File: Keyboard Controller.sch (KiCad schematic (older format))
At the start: 48 parts, among them SW1 SW_Push, SW2 SW_Push, SW3 SW_Push, SW4 SW_Push, SW5 SW_Push, SW6 SW_Push, SW7 SW_Push, SW8 SW_Push, SW9 SW_Push, U1 Teensy-3.2

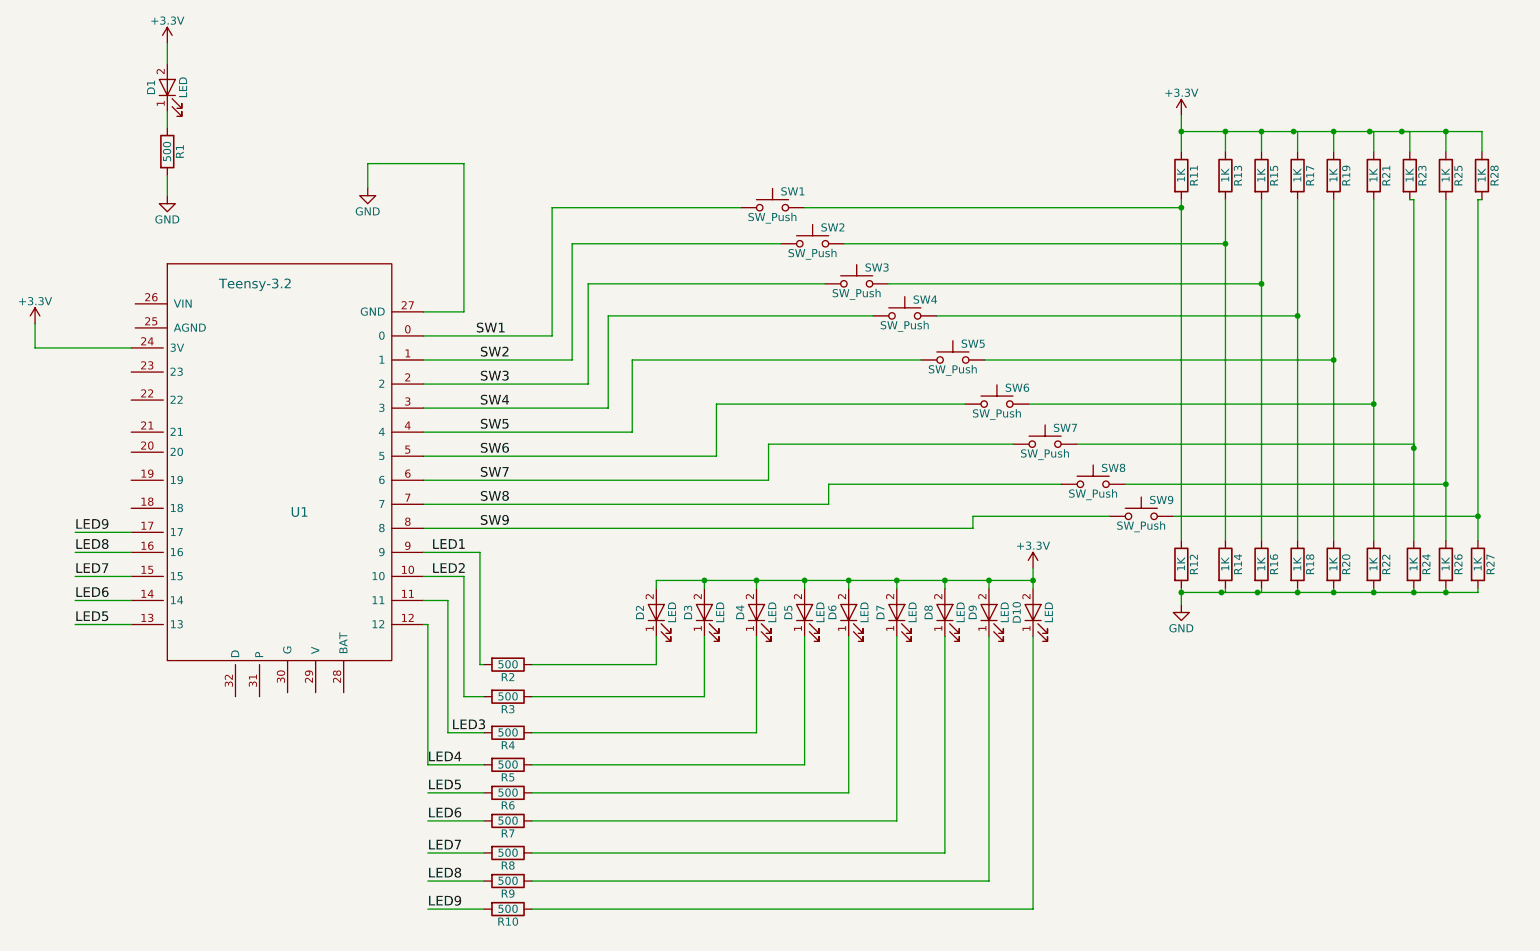
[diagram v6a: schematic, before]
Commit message: Changed pinout for easier layout
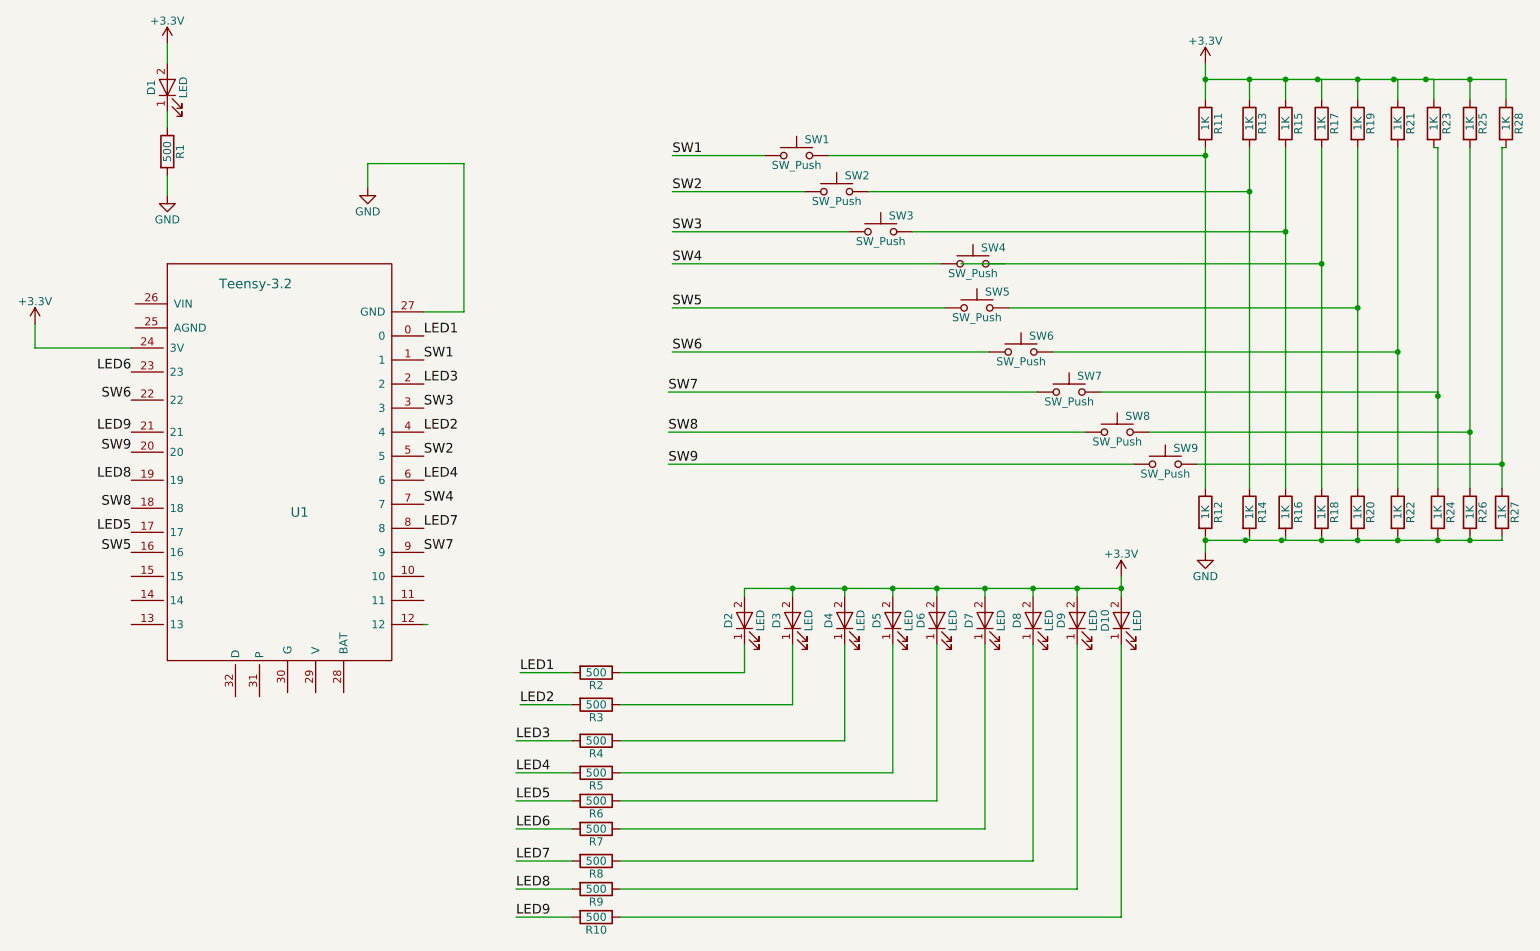
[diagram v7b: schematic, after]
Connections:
- net LED1: now also U1.0; no longer U1.9
- net LED2: now also U1.4; no longer U1.10
- net LED3: now also U1.2; no longer U1.11
- net LED4: now also U1.6; no longer U1.12
- net LED5: now also U1.17; no longer U1.13
- net LED6: now also U1.23; no longer U1.14
- net LED7: now also U1.8; no longer U1.15
- net LED8: now also U1.19; no longer U1.16
- net LED9: now also U1.21; no longer U1.17
- net SW1: now also U1.1; no longer U1.0
- net SW2: now also U1.5; no longer U1.1
- net SW3: now also U1.3; no longer U1.2
- net SW4: now also U1.7; no longer U1.3
- net SW5: now also U1.16; no longer U1.4
- net SW6: now also U1.22; no longer U1.5
- net SW7: now also U1.9; no longer U1.6
- net SW8: now also U1.18; no longer U1.7
- net SW9: now also U1.20; no longer U1.8
- net at R17.2, R18.1: no longer SW4.2
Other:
- moved on the sheet: D10, D2, D3, D4, D5, D6, D7, D8, D9, R10, R11, R12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

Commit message: Fixed ERC error
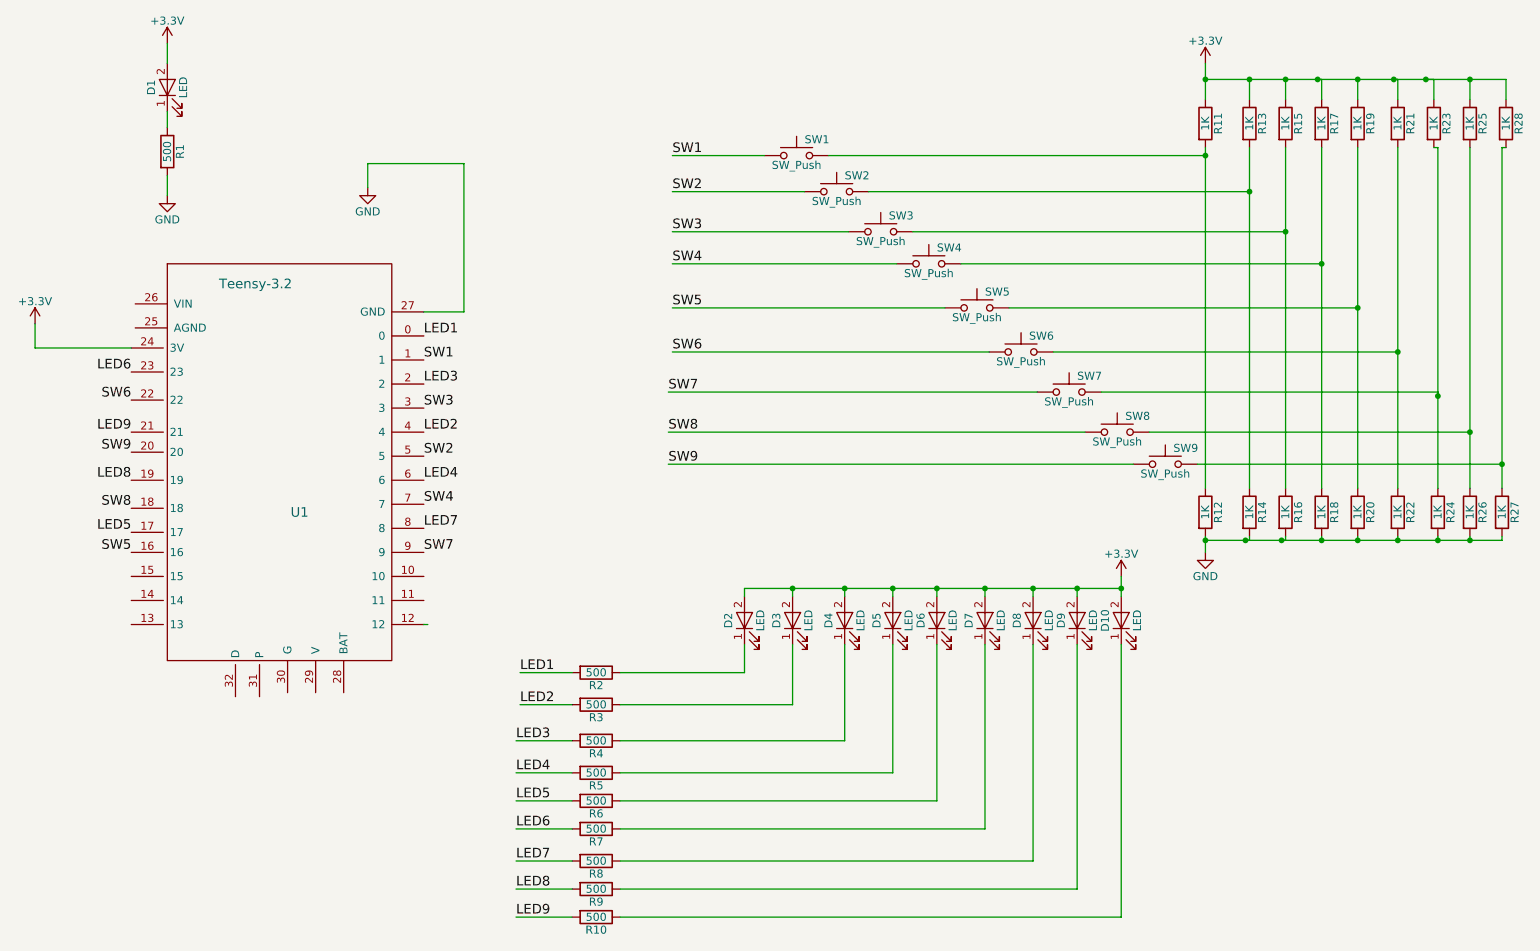
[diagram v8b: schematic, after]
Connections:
- net at SW4.2: now also R17.2, R18.1
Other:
- moved on the sheet: SW4
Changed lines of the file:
@@
 L SW_Push SW4
 U 1 1 586B3A7C
-P 7350 2325
-F 0 "SW4" H 7400 2425 50  0000 L CNN
-F 1 "SW_Push" H 7350 2265 50  0000 C CNN
-F 2 "Key:PTS645SK43SMTR92" H 7350 2525 50  0001 C CNN
-F 3 "" H 7350 2525 50  0000 C CNN
-F 4 "PTS645SK43SMTR92" H 7350 2325 60  0001 C CNN "MPN"
-	1    7350 2325
+P 7075 2325
+F 0 "SW4" H 7125 2425 50  0000 L CNN
+F 1 "SW_Push" H 7075 2265 50  0000 C CNN
+F 2 "Key:PTS645SK43SMTR92" H 7075 2525 50  0001 C CNN
+F 3 "" H 7075 2525 50  0000 C CNN
+F 4 "PTS645SK43SMTR92" H 7075 2325 60  0001 C CNN "MPN"
+	1    7075 2325
 	1    0    0    -1
 $EndComp
@@
 	2325 1775 2325 1900
 Wire Wire Line
-	8800 1075 8800 1175
-Wire Wire Line
-	8800 1175 8800 1300
-Wire Wire Line
-	8800 1600 8800 1650
-Wire Wire Line
-	8800 1650 8800 3725
-Wire Wire Line
-	8800 4025 8800 4050
-Wire Wire Line
-	8800 4050 8800 4125
+	8800 1075 8800 1300
+Wire Wire Line
+	8800 1600 8800 3725
+Wire Wire Line
+	8800 4025 8800 4125
 Wire Wire Line
 	6450 1650 8800 1650
@@
 	9075 1175 9075 1300
 Wire Wire Line
-	9075 1600 9075 1875
-Wire Wire Line
-	9075 1875 9075 3725
+	9075 1600 9075 3725
 Wire Wire Line
 	9300 1175 9300 1300
 Wire Wire Line
-	9300 1600 9300 2125
-Wire Wire Line
-	9300 2125 9300 3725
+	9300 1600 9300 3725
 Wire Wire Line
 	9525 1175 9525 1300
 Wire Wire Line
-	9525 1600 9525 2325
-Wire Wire Line
-	9525 2325 9525 3725
+	9525 1600 9525 3725
 Wire Wire Line
 	9750 1175 9750 1300
 Wire Wire Line
-	9750 1600 9750 2600
-Wire Wire Line
-	9750 2600 9750 3725
+	9750 1600 9750 3725
 Wire Wire Line
 	9075 4050 9075 4025
 Wire Wire Line
-	8800 4050 9050 4050
-Wire Wire Line
-	9050 4050 9075 4050
+	8800 4050 9075 4050
 Connection ~ 8800 4050
 Wire Wire Line
-	9050 4050 9275 4050
-Wire Wire Line
-	9275 4050 9300 4050
+	9050 4050 9300 4050
 Wire Wire Line
 	9300 4050 9300 4025
 Wire Wire Line
-	9275 4050 9525 4050
-Wire Wire Line
-	9525 4050 9750 4050
-Wire Wire Line
-	9750 4050 10000 4050
-Wire Wire Line
-	10000 4050 10250 4050
-Wire Wire Line
-	10250 4050 10450 4050
-Wire Wire Line
-	10450 4050 10650 4050
+	9275 4050 10650 4050
 Wire Wire Line
 	9525 4050 9525 4025
@@
 Connection ~ 9750 2600
 Wire Wire Line
-	8800 1175 9075 1175
-Wire Wire Line
-	9075 1175 9300 1175
-Wire Wire Line
-	9300 1175 9500 1175
-Wire Wire Line
-	9500 1175 9525 1175
+	8800 1175 9525 1175
 Connection ~ 8800 1175
 Connection ~ 9075 1175
 Connection ~ 9300 1175
 Wire Wire Line
-	9500 1175 9750 1175
-Wire Wire Line
-	9750 1175 9975 1175
-Wire Wire Line
-	9975 1175 10000 1175
+	9500 1175 10000 1175
 Connection ~ 9500 1175
 Wire Wire Line
@@
 Connection ~ 9750 1175
 Wire Wire Line
-	9975 1175 10175 1175
-Wire Wire Line
-	10175 1175 10225 1175
+	9975 1175 10225 1175
 Wire Wire Line
 	10225 1175 10225 1300
 Connection ~ 9975 1175
 Wire Wire Line
-	10175 1175 10450 1175
-Wire Wire Line
-	10450 1175 10675 1175
+	10175 1175 10675 1175
 Wire Wire Line
 	10450 1175 10450 1300
@@
 Connection ~ 10450 1175
 Wire Wire Line
-	10000 1600 10000 2875
-Wire Wire Line
-	10000 2875 10000 3725
+	10000 1600 10000 3725
 Wire Wire Line
 	10000 4050 10000 4025
@@
 Connection ~ 10450 4050
 Wire Wire Line
-	10250 1600 10250 3150
-Wire Wire Line
-	10250 3150 10250 3725
+	10250 1600 10250 3725
 Wire Wire Line
 	10225 1600 10250 1600
 Wire Wire Line
-	10450 1600 10450 3375
-Wire Wire Line
-	10450 3375 10450 3725
-Wire Wire Line
-	10650 1600 10650 3575
-Wire Wire Line
-	10650 3575 10650 3725
+	10450 1600 10450 3725
+Wire Wire Line
+	10650 1600 10650 3725
 Wire Wire Line
 	10650 1600 10675 1600
@@
 	5475 2125 6575 2125
 Wire Wire Line
-	5475 2325 7150 2325
-Wire Wire Line
 	5475 2600 7175 2600
 Wire Wire Line
@@
 	5450 3575 8350 3575
 Wire Wire Line
-	8275 4275 8275 4350
-Wire Wire Line
-	8275 4350 8275 4400
+	8275 4275 8275 4400
 Wire Wire Line
 	8275 4700 8275 6400
@@
 	8275 6400 5150 6400
 Wire Wire Line
-	5925 4350 6225 4350
-Wire Wire Line
-	6225 4350 6550 4350
-Wire Wire Line
-	6550 4350 6850 4350
-Wire Wire Line
-	6850 4350 7125 4350
-Wire Wire Line
-	7125 4350 7425 4350
-Wire Wire Line
-	7425 4350 7725 4350
-Wire Wire Line
-	7725 4350 8000 4350
-Wire Wire Line
-	8000 4350 8275 4350
+	5925 4350 8275 4350
 Wire Wire Line
 	5925 4350 5925 4400
@@
 Text Label 2100 4125 2    60   ~ 0
 SW5
+Wire Wire Line
+	6875 2325 5475 2325
 $EndSCHEMATC
